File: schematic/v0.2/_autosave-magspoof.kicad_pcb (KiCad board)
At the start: 2 copper layers, 29.2 x 39.4 mm, 23 parts, among them IC1 STM32F042G6U6, IC3 DRV8835DSSR, P1 USB_A, P2 Expansion Port, P3 Ext Clock, P4 Program Port, SW1 Select, SW2 FIRE!, U1 MCP73831-2-OT

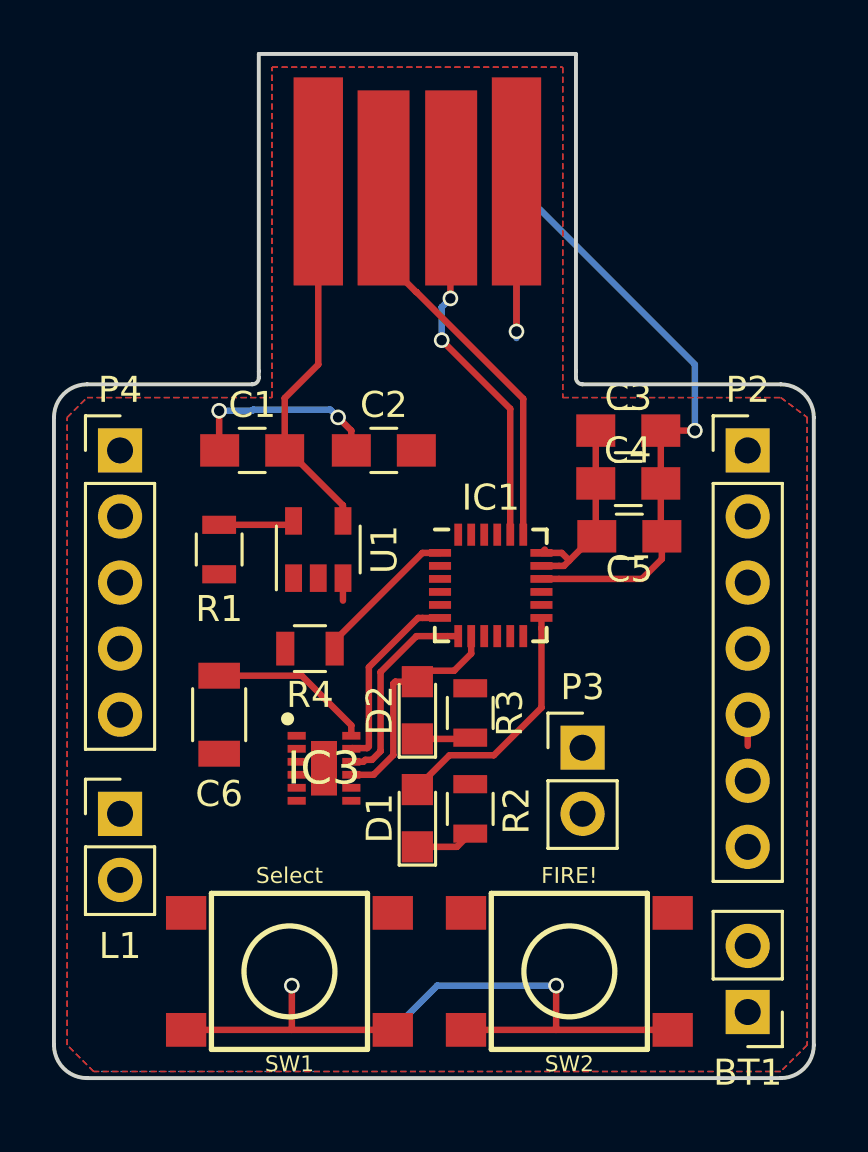
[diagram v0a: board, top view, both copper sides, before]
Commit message: Changed stm32 footprint
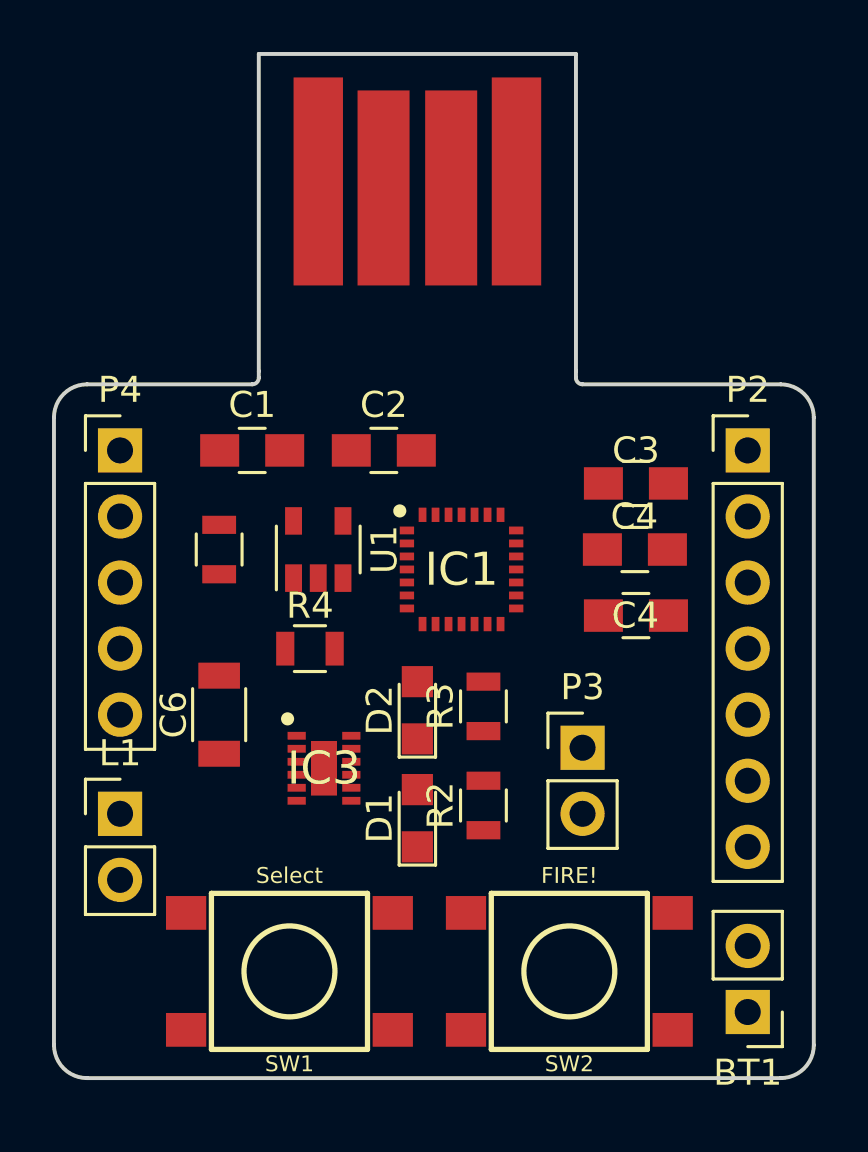
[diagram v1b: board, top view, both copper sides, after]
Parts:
- IC1: footprint Housings_DFN_QFN:QFN-24_4x4mm_Pitch0.5mm -> STM32F042G6U6:QFN50P400X400X60-28N
- moved C5 3.06 mm to (158.3, 106.7), turned to 180 degrees
- moved C4 2.55 mm to (158.2, 104.1)
- moved C3 2.05 mm to (158.3, 101.6)
- moved IC1 1.28 mm to (151.6, 104.9)
- moved R3 0.57 mm to (152.4, 110.2)
- moved R2 0.52 mm to (152.4, 114.0)
- turned R1 to 90 degrees
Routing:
- net GND: track 44.1 -> 0.00 mm, vias 4 -> 0
- net (no net): track 26.0 -> 0.00 mm, vias 2 -> 0
- net USB_DM: track 15.6 -> 0.00 mm
- net VCC: track 15.2 -> 0.00 mm
- net USB_VCC: track 14.6 -> 0.00 mm
- net SWCLK: track 14.6 -> 0.00 mm, vias 2 -> 0
- net LED2: track 9.58 -> 0.00 mm
- net LED1: track 8.82 -> 0.00 mm
- net Net-(IC1-Pad7): track 7.90 -> 0.00 mm
- net Net-(IC1-Pad6): track 7.28 -> 0.00 mm
- net Net-(IC1-Pad1): track 5.75 -> 0.00 mm
- net Net-(R1-Pad1): track 2.92 -> 0.00 mm
- net Net-(D1-Pad1): track 2.24 -> 0.00 mm
- net Net-(D2-Pad1): track 2.05 -> 0.00 mm
- net Net-(IC1-Pad26): track 1.20 -> 0.00 mm
- removed copper zone on B.Cu, net GND
- removed copper zone on F.Cu, net VCC
